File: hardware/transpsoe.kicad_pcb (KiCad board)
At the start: 2 copper layers, 102.2 x 51 mm, 107 parts, among them J1 AudioJack2_SwitchT, J10 AudioJack2_SwitchT, J11 AudioJack2_SwitchT, J12 Conn_01x08_Female, J13 Conn_01x08_Female, J14 Conn_01x08_Male, J15 Conn_01x08_Male, J2 AudioJack2_SwitchT, J3 AudioJack2_SwitchT, J4 AudioJack2_SwitchT, J5 AudioJack2_SwitchT, J6 AudioJack2_SwitchT, J7 Conn_02x05_Odd_Even, J8 AudioJack2_SwitchT, J9 AudioJack2_SwitchT, SW1 SW_Rotary12, SW2 SW_SPDT, U1 OPA4991, U2 OPA4991, U3 OPA4991, U4 LM4040DBZ-4.1, U5 OPA4991, U6 OPA4991

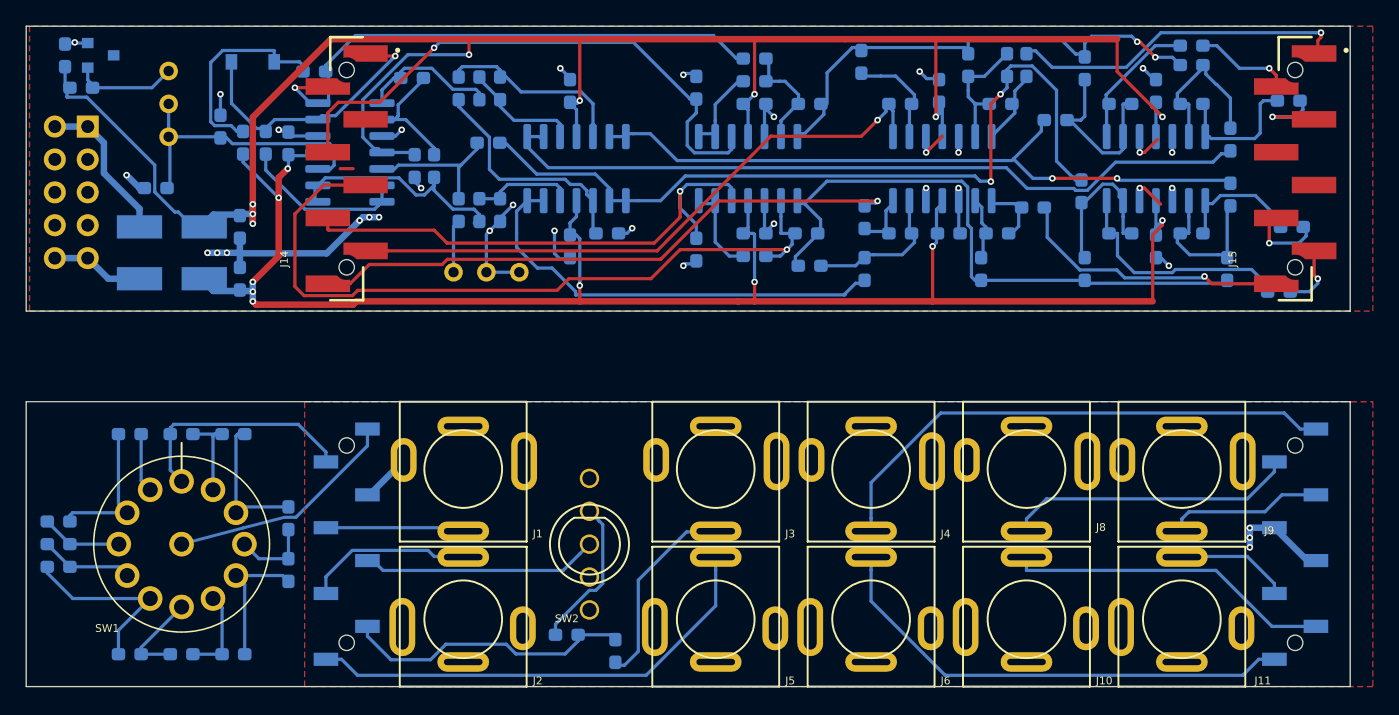
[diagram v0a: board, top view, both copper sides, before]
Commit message: Fix issues with board and bump rev
Errata fixed:
- C2 & R5 refdes were swapped on PCB
- R44 & R30 refdes were swapped on PCB
- R46 label off board
- D2 label off board
- C11 label on pad
- U4 label off board
- Fix via stitching on -12V

- Added rev marker to jack board
- Migrated to KiCad 6
- Added CHANGELOG.md
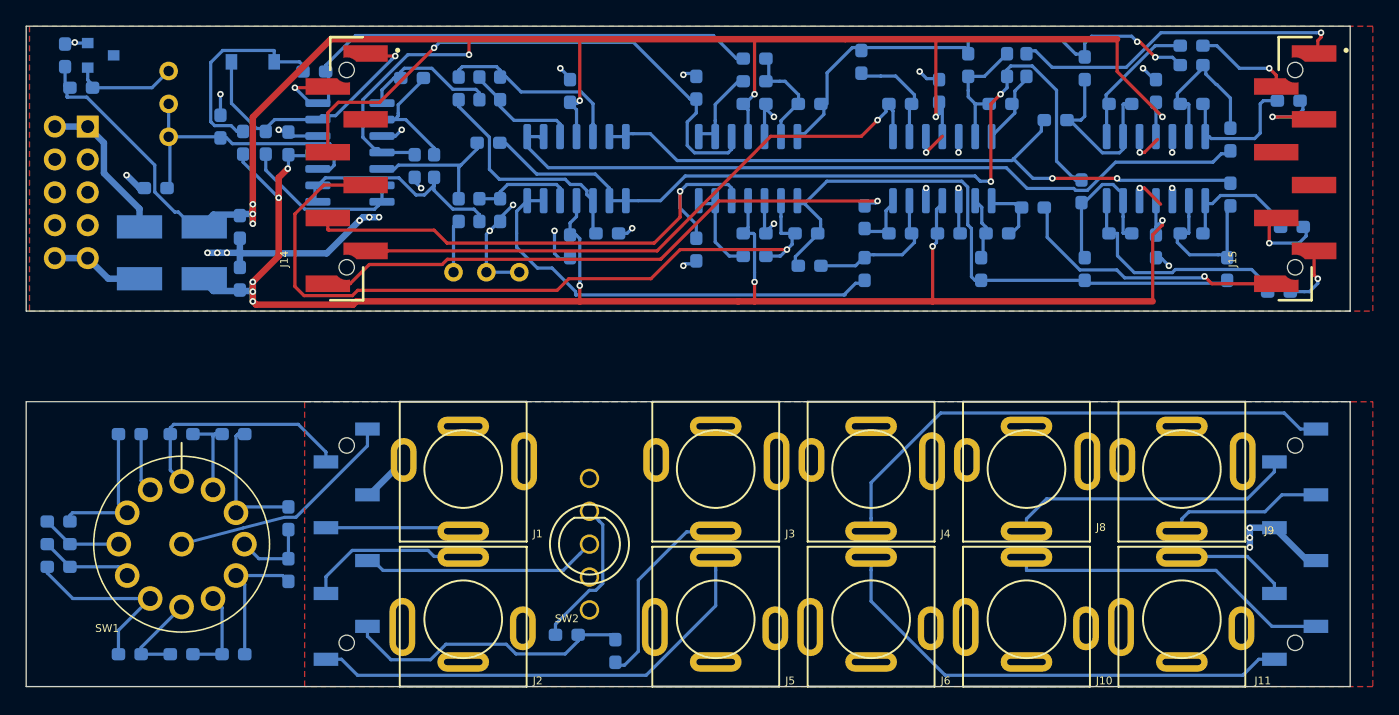
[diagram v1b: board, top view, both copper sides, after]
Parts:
- R24, R25, R26, R27, R44, R45, R46, R47: value 50 -> 51
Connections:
- J1 pad TN: Net-(J1-PadTN) -> unconnected-(J1-PadTN)
- J10 pad TN: Net-(J10-PadTN) -> unconnected-(J10-PadTN)
- J11 pad TN: Net-(J11-PadTN) -> unconnected-(J11-PadTN)
- J2 pad TN: Net-(J2-PadTN) -> unconnected-(J2-PadTN)
- J3 pad TN: Net-(J3-PadTN) -> unconnected-(J3-PadTN)
- J4 pad TN: Net-(J4-PadTN) -> unconnected-(J4-PadTN)
- J5 pad TN: Net-(J5-PadTN) -> unconnected-(J5-PadTN)
- J6 pad TN: Net-(J6-PadTN) -> unconnected-(J6-PadTN)
- J8 pad TN: Net-(J8-PadTN) -> unconnected-(J8-PadTN)
- J9 pad TN: Net-(J9-PadTN) -> unconnected-(J9-PadTN)
- SW2 pad 1: Net-(SW2-Pad1) -> unconnected-(SW2-Pad1)
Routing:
- net Net-(R32-Pad1): track 13.1 -> 10.9 mm
- net Net-(R51-Pad2): track 18.7 -> 17.2 mm
- net GND: track 75.3 -> 73.9 mm
- net -12V: track 128.7 -> 129.7 mm
- net Net-(D2-Pad1): track 8.02 -> 7.20 mm
- net Net-(D1-Pad2): track 12.7 -> 11.9 mm
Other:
- net class Default removed
- board text added: "rev 1"
- board text removed: "rev 0"

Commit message: Fix 3d models and migrate to KiCad6 R/C footprints
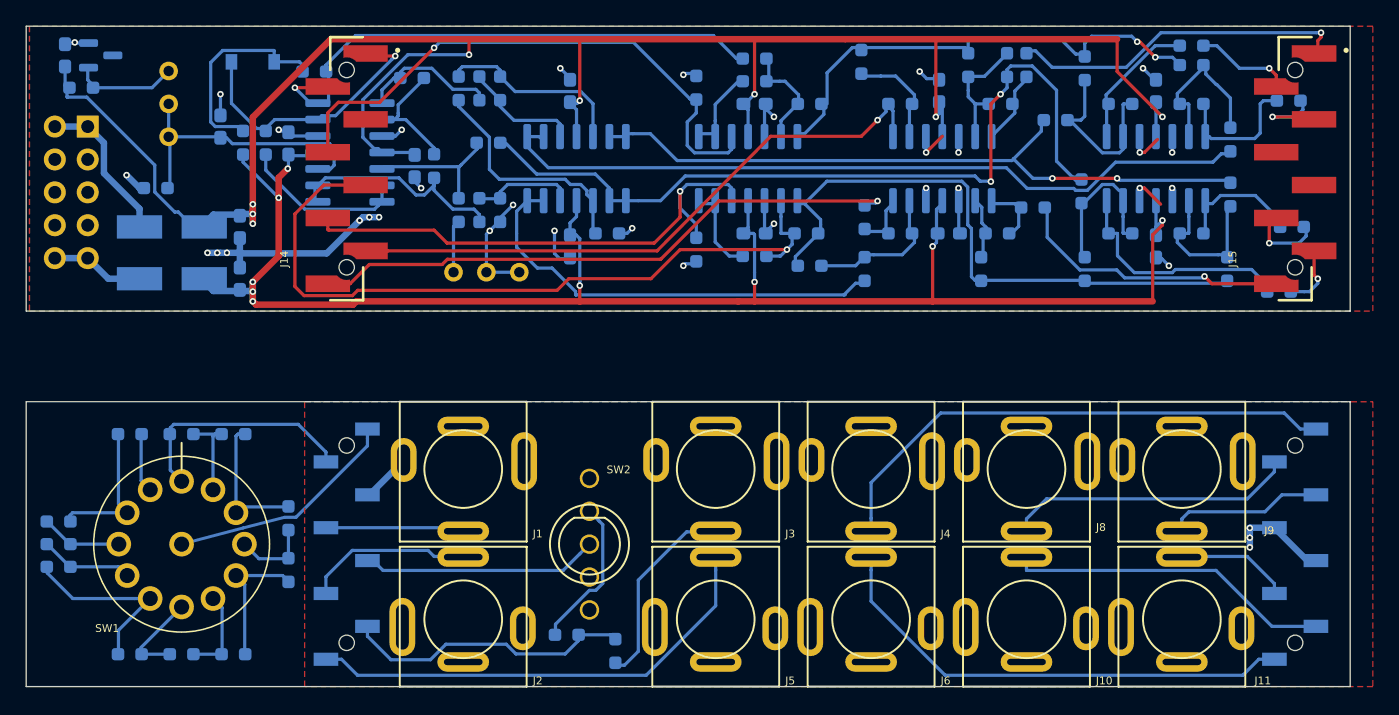
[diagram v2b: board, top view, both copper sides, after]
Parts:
- C1, C10, C11, C12, C13, C14, C2, C3, C4, C5, C6, C7, C8, C9: footprint Capacitor_SMD:C_0603_1608Metric_Pad1.05x0.95mm_HandSolder -> Capacitor_SMD:C_0603_1608Metric_Pad1.08x0.95mm_HandSolder
- R1, R10, R11, R12, R13, R14, R16, R2, R20, R21, R22, R23, R24, R25, R26, R27, R28, R29, R30, R31, R32, R33, R34, R35, R4, R40, R41, R42, R43, R44, R45, R46, R47, R48, R49, R5, R50, R51, R52, R53, R54, R55, R56, R57, R58, R6, R67, R68, R69, R7, R70, R71, R72, R73, R74, R75, R76, R77, R78, R79, R80, R81, R82, R9: footprint Resistor_SMD:R_0603_1608Metric_Pad1.05x0.95mm_HandSolder -> Resistor_SMD:R_0603_1608Metric_Pad0.98x0.95mm_HandSolder
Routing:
- net +12V: track 157.5 -> 154.8 mm
- net GND: track 73.9 -> 71.9 mm
- net SW1.b: track 42.5 -> 40.9 mm
- net /J2.T: track 41.6 -> 40.6 mm
- net /J1.T: track 45.2 -> 44.1 mm
- net Jacks-GND: track 11.6 -> 10.7 mm
- net Net-(R80-Pad2): track 10.9 -> 10.3 mm

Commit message: Redesign output circuits
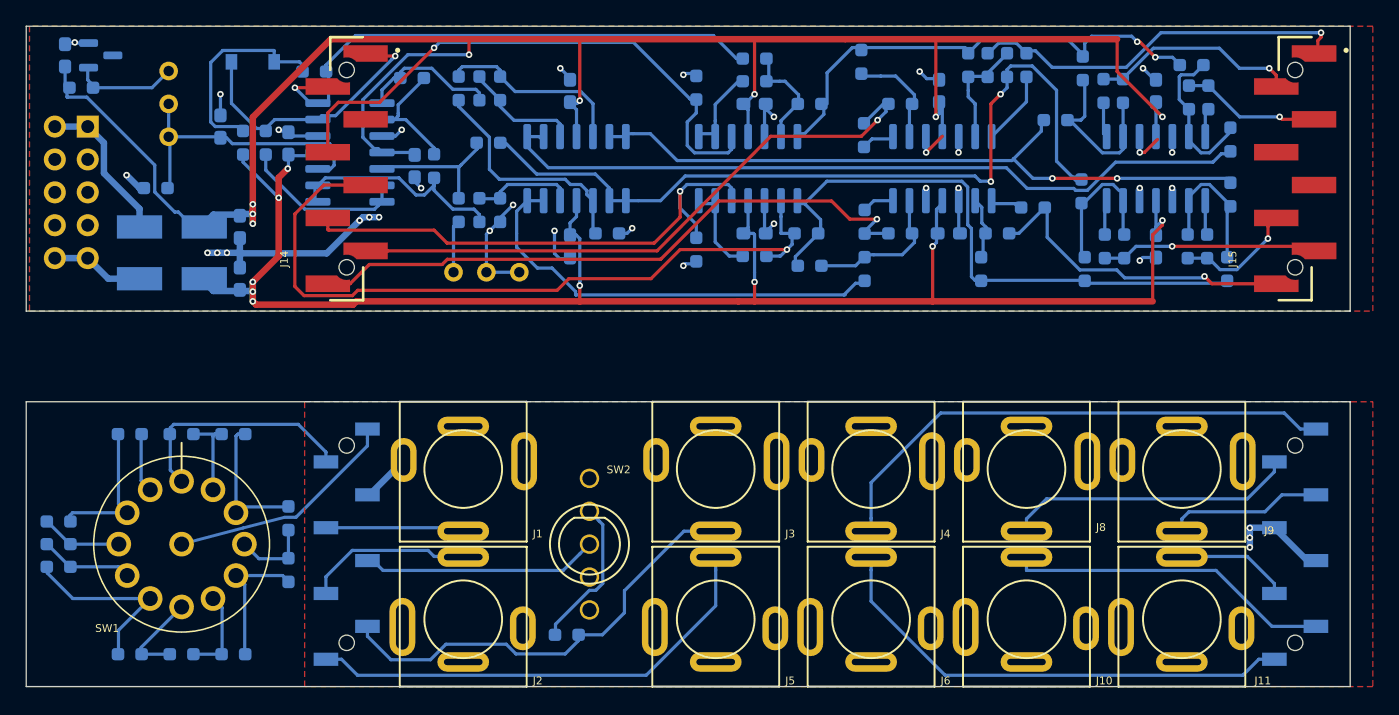
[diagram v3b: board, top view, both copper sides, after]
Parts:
- R24, R25, R26, R27, R44, R45, R46, R47: value 51 -> 330
- moved R24 44.2 mm to (164.7, 79.7), turned to -90 degrees
- moved R46 13.9 mm to (183.3, 88.2), turned to -90 degrees
- moved R44 7.65 mm to (183.2, 76.2), turned to 90 degrees
- moved R47 6.72 mm to (191.2, 88.2), turned to -90 degrees
- moved R45 6.21 mm to (191.3, 76.8), turned to 90 degrees
- moved R21 3.16 mm to (174.2, 74.2), turned to -90 degrees
- moved R42 1.04 mm to (184.8, 88.2), turned to 90 degrees
- moved R43 1.04 mm to (189.7, 88.2), turned to 90 degrees
- moved R40 1.02 mm to (184.7, 76.2), turned to -90 degrees
- moved R41 0.54 mm to (189.8, 76.8), turned to -90 degrees
- moved R26 0.35 mm to (164.8, 86.3), turned to -90 degrees
- moved R29 0.15 mm to (181.6, 74.5)
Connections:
- J3 pad T: Net-(J3-PadT) -> Jacks-A+S
- R21 pad 1: Net-(R21-Pad1) -> /J4.T
- R22 pad 1: Net-(R22-Pad1) -> /J5.T
- R23 pad 1: Net-(R23-Pad1) -> /J6.T
- R24 pad 1: Net-(J3-PadT) -> /A+S
- R24 pad 2: Jacks-A+S -> Net-(U2-Pad1)
- R25 pad 1: Net-(R21-Pad1) -> Net-(R25-Pad1)
- R26 pad 1: Net-(R22-Pad1) -> Net-(R26-Pad1)
- R27 pad 1: Net-(R23-Pad1) -> Net-(R27-Pad1)
- R40 pad 1: Net-(R40-Pad1) -> /J8.T
- R41 pad 1: Net-(R41-Pad1) -> /J9.T
- R42 pad 1: Net-(R42-Pad1) -> /J10.T
- R43 pad 1: Net-(R43-Pad1) -> /J11.T
- R44 pad 1: Net-(R40-Pad1) -> Net-(R44-Pad1)
- R45 pad 1: Net-(R41-Pad1) -> Net-(R45-Pad1)
- R46 pad 1: Net-(R42-Pad1) -> Net-(R46-Pad1)
- R47 pad 1: Net-(R43-Pad1) -> Net-(R47-Pad1)
- U2 pad 1: /A+S -> Net-(U2-Pad1)
- U2 pad 14: Net-(R22-Pad1) -> Net-(R26-Pad1)
- U2 pad 7: Net-(R21-Pad1) -> Net-(R25-Pad1)
- U2 pad 8: Net-(R23-Pad1) -> Net-(R27-Pad1)
- U3 pad 1: Net-(R40-Pad1) -> Net-(R44-Pad1)
- U3 pad 14: Net-(R42-Pad1) -> Net-(R46-Pad1)
- U3 pad 7: Net-(R41-Pad1) -> Net-(R45-Pad1)
- U3 pad 8: Net-(R43-Pad1) -> Net-(R47-Pad1)
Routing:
- net Net-(R42-Pad1): track 18.1 -> 0.00 mm
- net Net-(J3-PadT): track 15.2 -> 0.00 mm
- net /J10.T: track 4.79 -> 16.7 mm
- net Jacks-A+S: track 22.5 -> 34.4 mm
- net Net-(R41-Pad1): track 10.2 -> 0.00 mm
- net Net-(R40-Pad1): track 10.0 -> 0.00 mm
- net Net-(R43-Pad1): track 9.53 -> 0.00 mm
- net /J8.T: track 7.25 -> 16.1 mm
- net Net-(R25-Pad1): track 0.00 -> 5.73 mm
- net Net-(R21-Pad1): track 5.43 -> 0.00 mm
- net Net-(R23-Pad1): track 4.44 -> 0.00 mm
- net /J9.T: track 6.30 -> 10.7 mm
- net Net-(R22-Pad1): track 4.02 -> 0.00 mm
- net /J4.T: track 26.0 -> 29.6 mm
- net /J6.T: track 21.6 -> 25.2 mm
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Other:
- board text added: "rev 2"
